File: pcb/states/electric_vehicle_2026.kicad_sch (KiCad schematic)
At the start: 7 parts, among them J1 goBILDA Odometry Computer, M1 Motor_Servo_SuperSpeed, M2 Motor_Servo_Speed, SW1 SW_Push_Dual, SW2 Rotary_Encoder_SuperSpeed, SW3 Rotary_Encoder_Speed

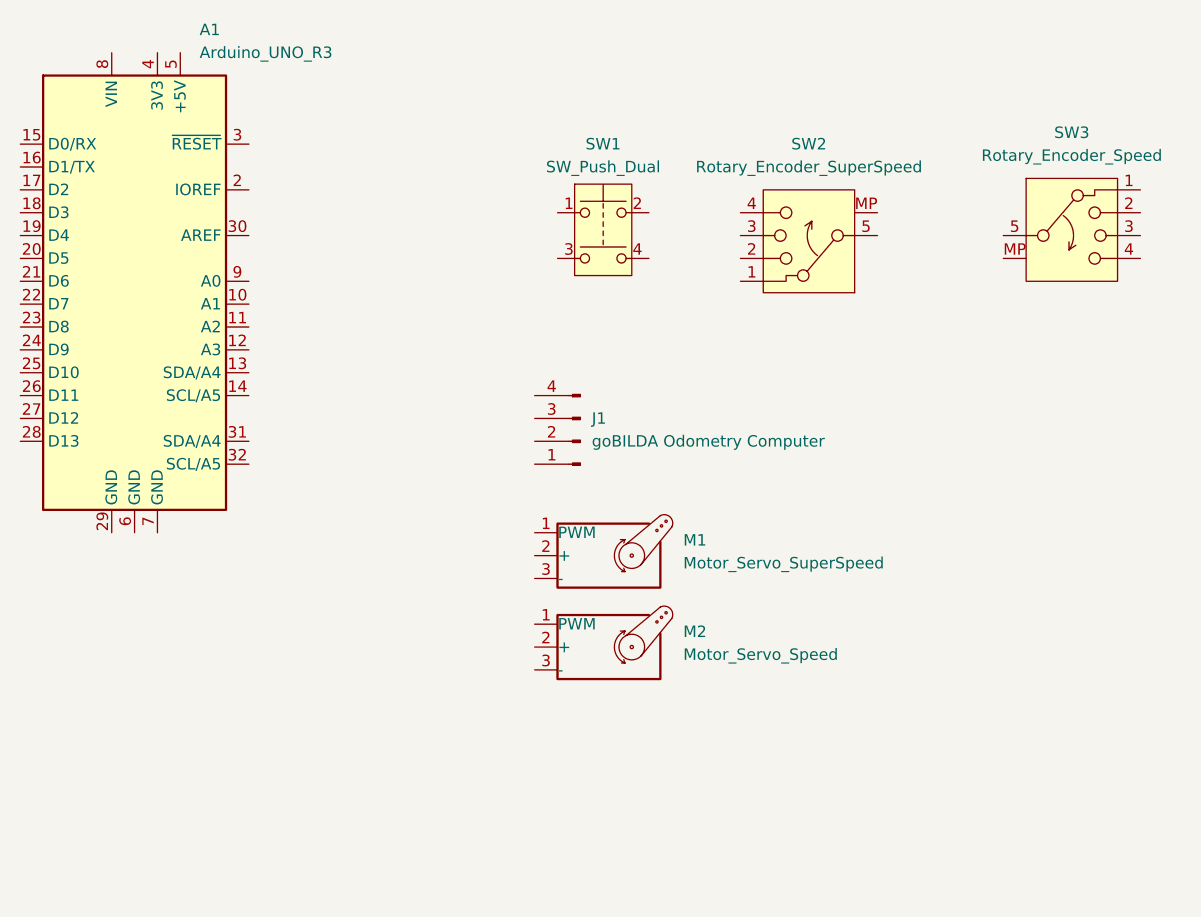
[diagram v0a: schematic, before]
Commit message: change schematic for states
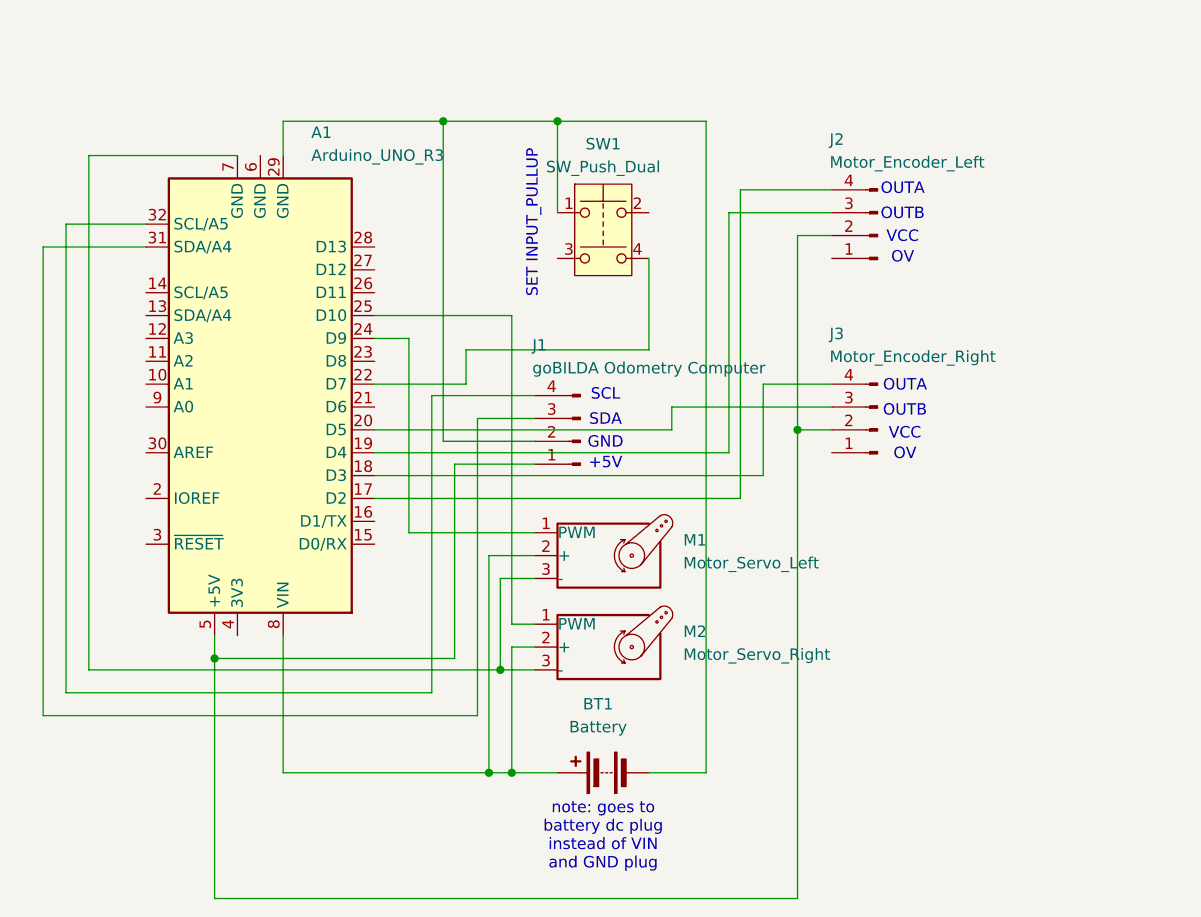
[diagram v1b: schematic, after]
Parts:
- removed SW2: Rotary_Encoder_SuperSpeed, symbol Switch:SW_Rotary_1x4_MP
- removed SW3: Rotary_Encoder_Speed, symbol Switch:SW_Rotary_1x4_MP
- added BT1: Battery, symbol Device:Battery
- added J2: Motor_Encoder_Left, symbol Connector:Conn_01x04_Pin
- added J3: Motor_Encoder_Right, symbol Connector:Conn_01x04_Pin
- M1: value Motor_Servo_SuperSpeed -> Motor_Servo_Left
- M2: value Motor_Servo_Speed -> Motor_Servo_Right
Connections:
- net at J1.1 (Pin_1): now also A1.5 (+5V), J2.2 (Pin_2), J3.2 (Pin_2)
- net at J1.2 (Pin_2): now also A1.29 (GND), SW1.1, BT1.2 (-)
- net at J1.3 (Pin_3): now also A1.31 (SDA/A4)
- net at J1.4 (Pin_4): now also A1.32 (SCL/A5)
- net at M2.1 (PWM): now also A1.25 (D10)
- net at M2.2 (+): now also A1.8 (VIN), M1.2 (+), BT1.1 (+)
- net at M2.3 (-): now also A1.7 (GND), M1.3 (-)
- net at M1.1 (PWM): now also A1.24 (D9)
- net at A1.17 (D2): now also J2.4 (Pin_4)
- net at A1.18 (D3): now also J3.4 (Pin_4)
- net at A1.19 (D4): now also J2.3 (Pin_3)
- net at A1.20 (D5): now also J3.3 (Pin_3)
- net at A1.22 (D7): now also SW1.4
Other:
- note added: "+5V"
- note added: "GND"
- note added: "OUTA"
- note added: "OUTB"
- note added: "OV"
- note added: "SCL"
- note added: "SDA"
- note added: "SET INPUT_PULLUP"
- note added: "VCC"
- note added: "note: goes to battery dc plug instead of VIN and GND plug"
- moved on the sheet: A1
